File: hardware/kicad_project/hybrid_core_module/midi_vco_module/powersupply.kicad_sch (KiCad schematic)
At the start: 64 parts, among them J7 USB_C_Receptacle_USB2.0_14P, J8 Conn_02x08_Odd_Even_MountingP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, Q1 2N7002, U16 MC79M12CDTRKG, U3 USBLC6-2SC6, U4 TPS65131TRGERQ1, U5 MC78M12CDTRKG, U6 DS-9536, U7 6N137, U8 AZ1117CH2-3.3

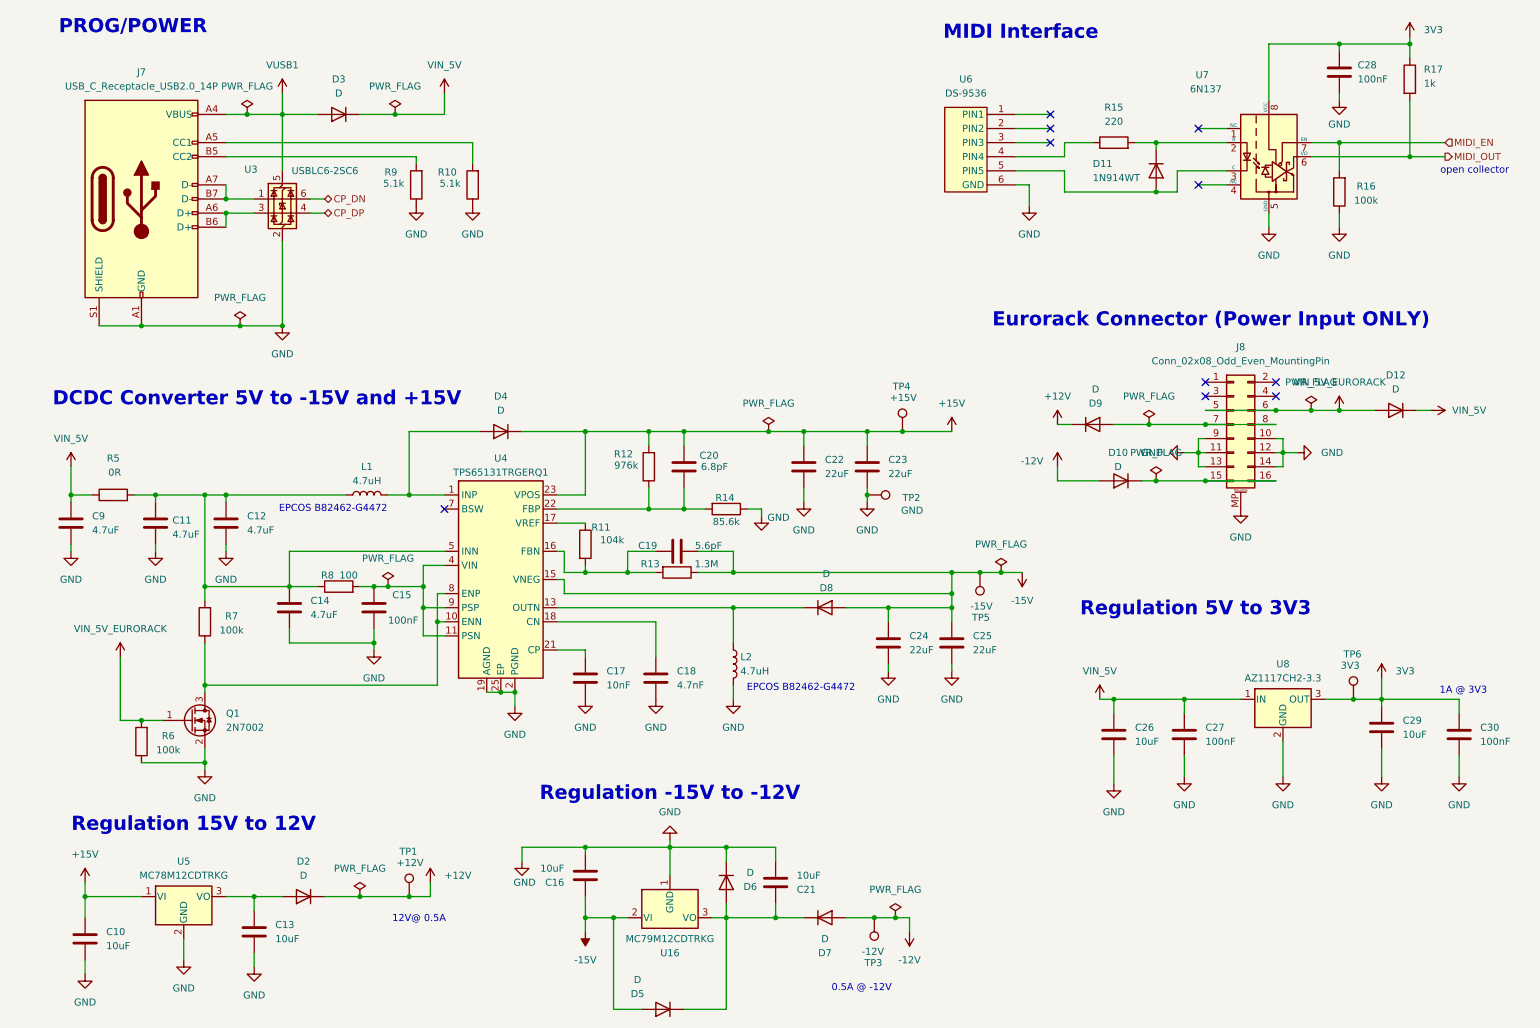
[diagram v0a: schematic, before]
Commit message: Schematic updated. Components Footprint assignment started. Waiting for components mechanical validation before starting layout.
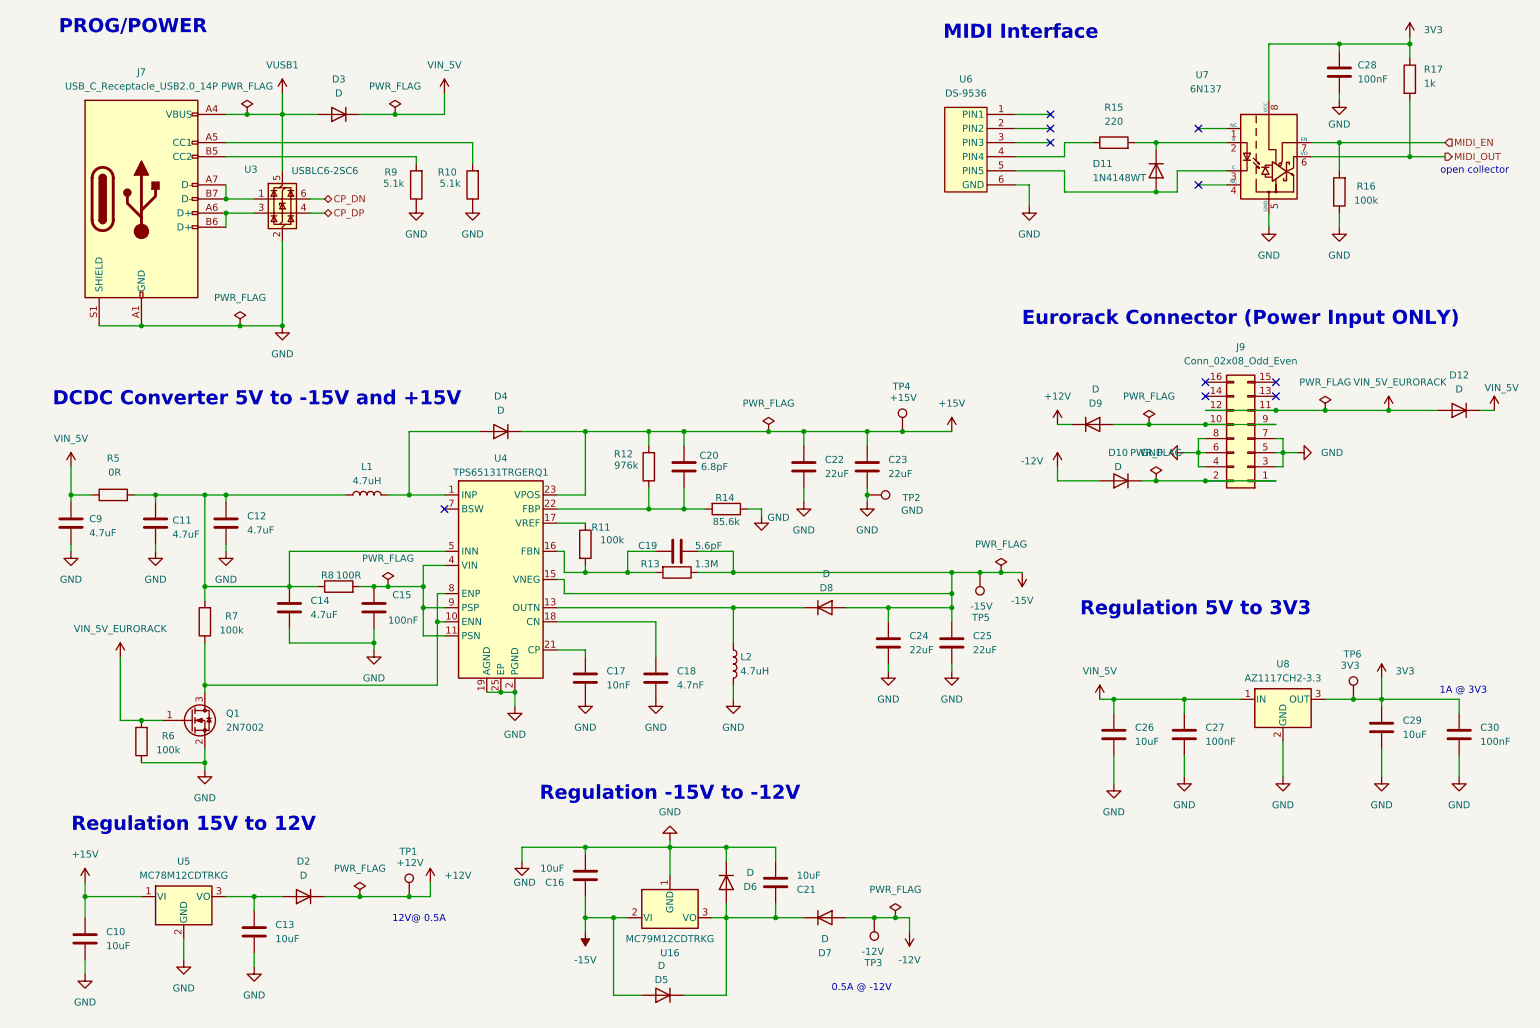
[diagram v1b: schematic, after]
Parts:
- removed J8: Conn_02x08_Odd_Even_MountingPin, symbol Connector_Generic_MountingPin:Conn_02x08_Odd_Even_MountingPin
- added J9: Conn_02x08_Odd_Even, Connector_PinHeader_2.54mm:PinHeader_2x08_P2.54mm_Vertical, symbol Connector_Generic:Conn_02x08_Odd_Even
- C10, C13, C16, C21, C26, C29: footprint Capacitor_SMD:C_0402_1005Metric -> Capacitor_SMD:C_0805_2012Metric; Manufacturer (none) -> MURATA; Manufacturer PartNumer (none) -> GRM21BR61E106KA73K
- C11, C12, C14: footprint (none) -> Capacitor_SMD:C_0805_2012Metric; Manufacturer (none) -> MURATA; Manufacturer PartNumer (none) -> GRM219R61E475MA73D
- C15, C27, C28, C30: footprint (none) -> Capacitor_SMD:C_0402_1005Metric; Manufacturer (none) -> MURATA; Manufacturer PartNumer (none) -> GRM155R71E104KE14J
- C17: footprint (none) -> Capacitor_SMD:C_0402_1005Metric; Manufacturer (none) -> MURATA; Manufacturer PartNumer (none) -> GRM155R71E103KA01D
- C18: footprint (none) -> Capacitor_SMD:C_0402_1005Metric; Manufacturer (none) -> MURATA; Manufacturer PartNumer (none) -> GRM155R71E472KA01J
- C19: footprint (none) -> Capacitor_SMD:C_0402_1005Metric; Manufacturer (none) -> MURATA; Manufacturer PartNumer (none) -> GJM1555C1H5R6BB01J
- C20: footprint (none) -> Capacitor_SMD:C_0402_1005Metric; Manufacturer (none) -> MURATA; Manufacturer PartNumer (none) -> GJM1555C1H6R8DB01D
- C22, C23, C24, C25: footprint (none) -> Capacitor_SMD:C_1210_3225Metric; Manufacturer (none) -> SAMSUNG; Manufacturer PartNumer (none) -> CL32A226KAJNNNE
- C9: footprint Resistor_SMD:R_0402_1005Metric -> Capacitor_SMD:C_0805_2012Metric; Manufacturer (none) -> MURATA; Manufacturer PartNumer (none) -> GRM219R61E475MA73D
- D10, D12, D2, D3, D4, D5, D6, D7, D8, D9: footprint (none) -> Diode_SMD:D_Powermite_AK; Manufacturer (none) -> ONSEMI
- D11: value 1N914WT -> 1N4148WT; Manufacturer (none) -> ONSEMI/FAIRCHILD; Manufacturer PartNumer (none) -> 1N4148WT
- J7: footprint (none) -> Connector_USB:USB_C_Receptacle_G-Switch_GT-USB-7051x; Manufacturer (none) -> G-Switch; Manufacturer PartNumer (none) -> GT-USB-7051A
- L1, L2: footprint (none) -> Inductor_SMD:L_TDK_SLF6028; Manufacturer (none) -> TDK; Manufacturer PartNumer EPCOS B82462-G4472 -> SLF6028T-4R7M1R6-PF
- R10: footprint (none) -> Resistor_SMD:R_0402_1005Metric; Manufacturer (none) -> YAGEO; Manufacturer PartNumer (none) -> RT0402FRE075K1L
- R11: value 104k -> 100k; footprint (none) -> Resistor_SMD:R_0402_1005Metric; Manufacturer (none) -> YAGEO; Manufacturer PartNumer (none) -> RT0402FRE07100KL
- R12: footprint (none) -> Resistor_SMD:R_1206_3216Metric; Manufacturer (none) -> YAGEO; Manufacturer PartNumer (none) -> RT1206FRE07976KL
- R13: footprint (none) -> Resistor_SMD:R_0805_2012Metric; Manufacturer (none) -> YAGEO; Manufacturer PartNumer (none) -> RC0805FR-071M3L
- R14: footprint (none) -> Resistor_SMD:R_0402_1005Metric; Manufacturer (none) -> YAGEO; Manufacturer PartNumer (none) -> RT0402BRE0785K6L
- R15: footprint (none) -> Resistor_SMD:R_0402_1005Metric; Manufacturer (none) -> YAGEO; Manufacturer PartNumer (none) -> RT0402FRE07220RL
- R16, R6, R7: footprint (none) -> Resistor_SMD:R_0402_1005Metric; Manufacturer (none) -> YAGEO; Manufacturer PartNumer (none) -> RT0402FRE07100KL
- R17: footprint (none) -> Resistor_SMD:R_0402_1005Metric; Manufacturer (none) -> YAGEO; Manufacturer PartNumer (none) -> RT0402FRE071KL
- R5: footprint (none) -> Resistor_SMD:R_0402_1005Metric; Manufacturer (none) -> YAGEO; Manufacturer PartNumer (none) -> RC0402FR-070RL
- R8: value 100 -> 100R; footprint (none) -> Resistor_SMD:R_0402_1005Metric; Manufacturer (none) -> YAGEO; Manufacturer PartNumer (none) -> RT0402FRE07100RL
- R9: Manufacturer (none) -> YAGEO; Manufacturer PartNumer (none) -> RT0402FRE075K1L
- TP1, TP2, TP3, TP4, TP5, TP6: now left out of the parts list
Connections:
- net GND: now also J9.3 (Pin_3), J9.4 (Pin_4), J9.5 (Pin_5), J9.6 (Pin_6), J9.7 (Pin_7), J9.8 (Pin_8)
- net VIN_5V_EURORACK: now also J9.11 (Pin_11), J9.12 (Pin_12)
- net at D10.1 (K): now also J9.1 (Pin_1), J9.2 (Pin_2)
- net at D9.2 (A): now also J9.10 (Pin_10), J9.9 (Pin_9)
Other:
- note removed: "EPCOS B82462-G4472"
- moved on the sheet: D12, D5

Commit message: - schematic updated  - PN and footprints added
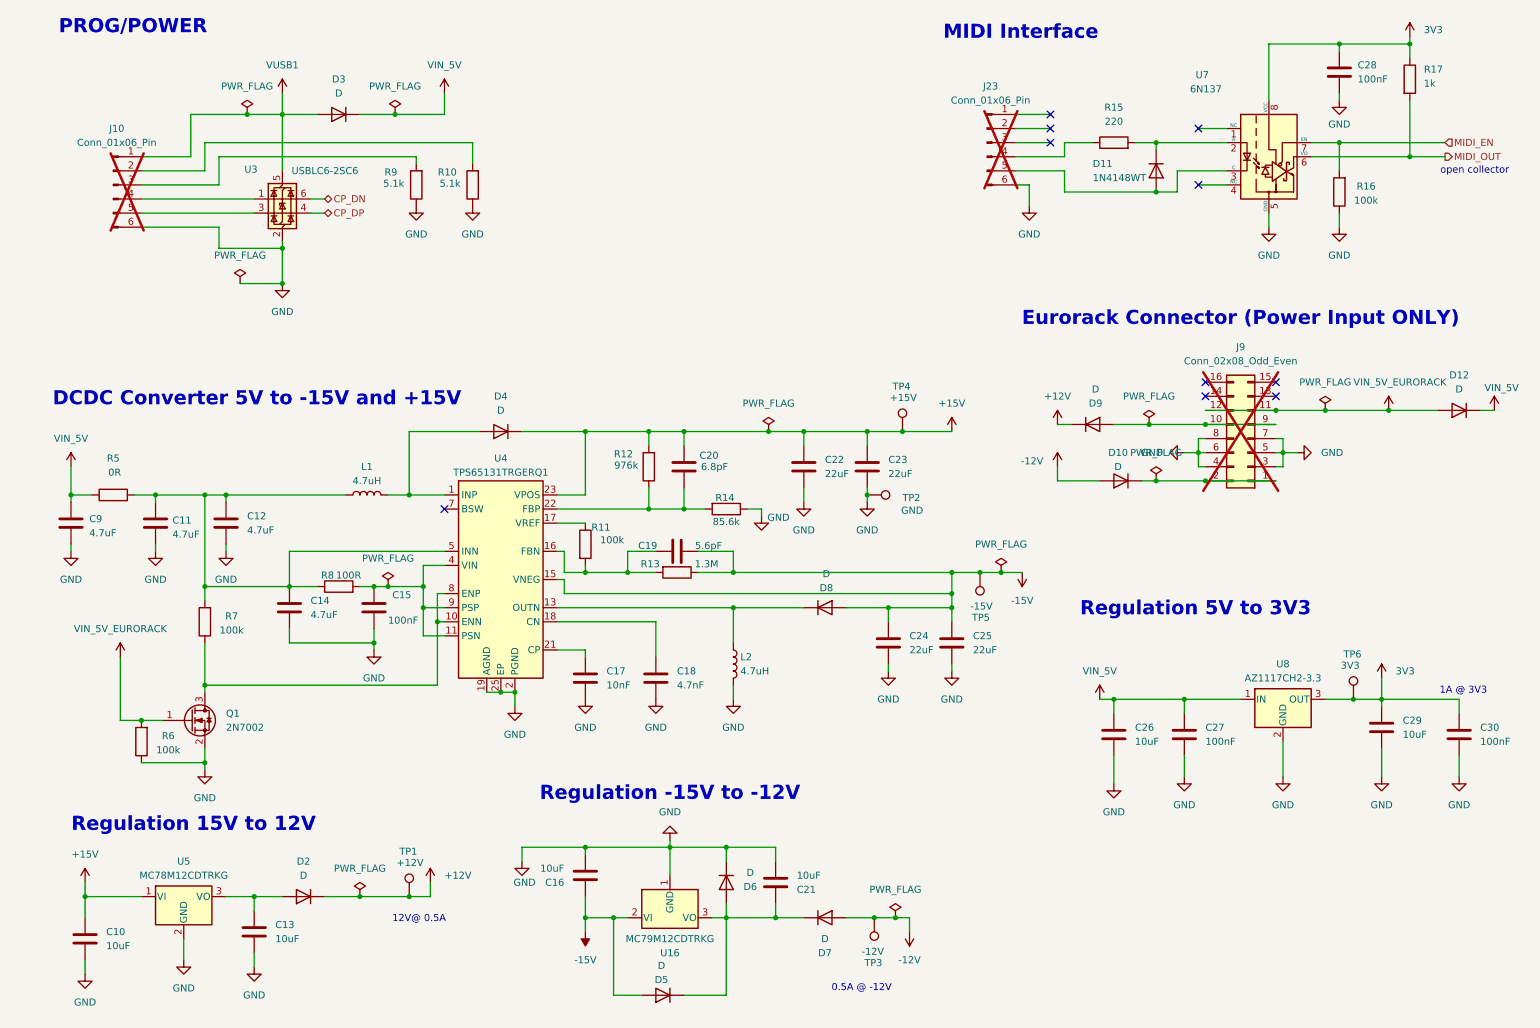
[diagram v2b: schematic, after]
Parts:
- removed J7: USB_C_Receptacle_USB2.0_14P, Connector_USB:USB_C_Receptacle_G-Switch_GT-USB-7051x, symbol Connector:USB_C_Receptacle_USB2.0_14P
- removed U6: DS-9536, symbol mylib:DS-9536
- added J10, J23: Conn_01x06_Pin, Connector_PinHeader_1.00mm:PinHeader_1x01_P1.00mm_Vertical, symbol Connector:Conn_01x06_Pin
- J9: now not fitted
- Q1: Manufacturer (none) -> onsemi; Manufacturer PartNumer (none) -> 2N7002
- U16: Manufacturer (none) -> onsemi; Manufacturer PartNumer (none) -> MC79M12CDTRKG
- U3: Manufacturer (none) -> STMicroelectronics; Manufacturer PartNumer (none) -> USBLC6-2SC6
- U4: Manufacturer (none) -> Texas Instruments; Manufacturer PartNumer (none) -> TPS65131TRGERQ1
- U5: Manufacturer (none) -> onsemi; Manufacturer PartNumer (none) -> MC78M12CDTRKG
- U8: Manufacturer (none) -> Diodes Incorporated; Manufacturer PartNumer (none) -> AZ1117CH2-3.3TRG1
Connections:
- net GND: now also J10.6 (Pin_6), J23.6 (Pin_6)
- net VUSB1: now also J10.1 (Pin_1)
- net at R10.2: now also J10.2 (Pin_2)
- net at U3.3 (I/O2): now also J10.5 (Pin_5)
- net at U3.1 (I/O1): now also J10.4 (Pin_4)
- net at R9.2: now also J10.3 (Pin_3)
- net at R15.1: now also J23.4 (Pin_4)
- net at D11.2 (A), U7.3 (C): now also J23.5 (Pin_5)
